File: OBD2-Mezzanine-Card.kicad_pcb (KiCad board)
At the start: 2 copper layers, 85 x 54 mm, 6 parts, among them P1 CONN_02X20, P2 CONN_02X20

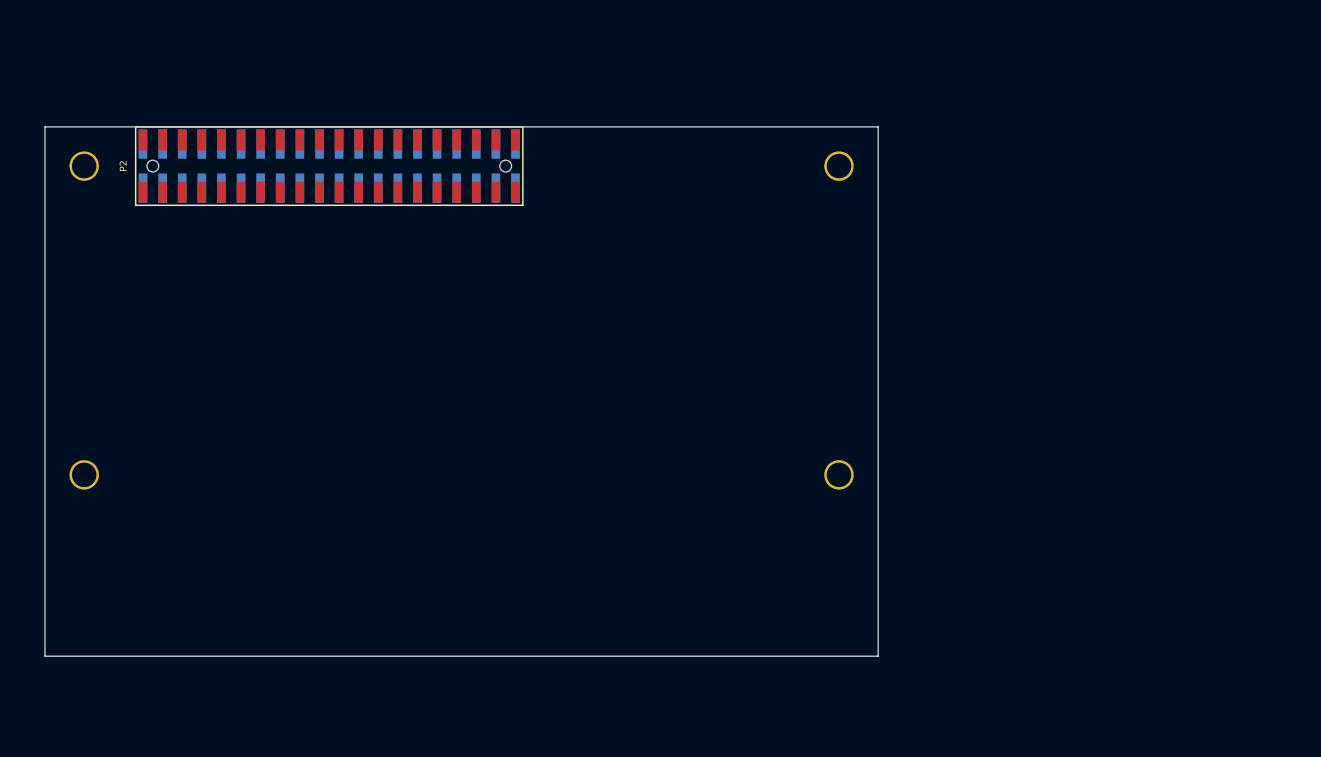
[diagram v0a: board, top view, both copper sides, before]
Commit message: kicad_pcd: Start to put the PCB together
Signed-off-by: Alistair Francis <alistair@alistair23.me>
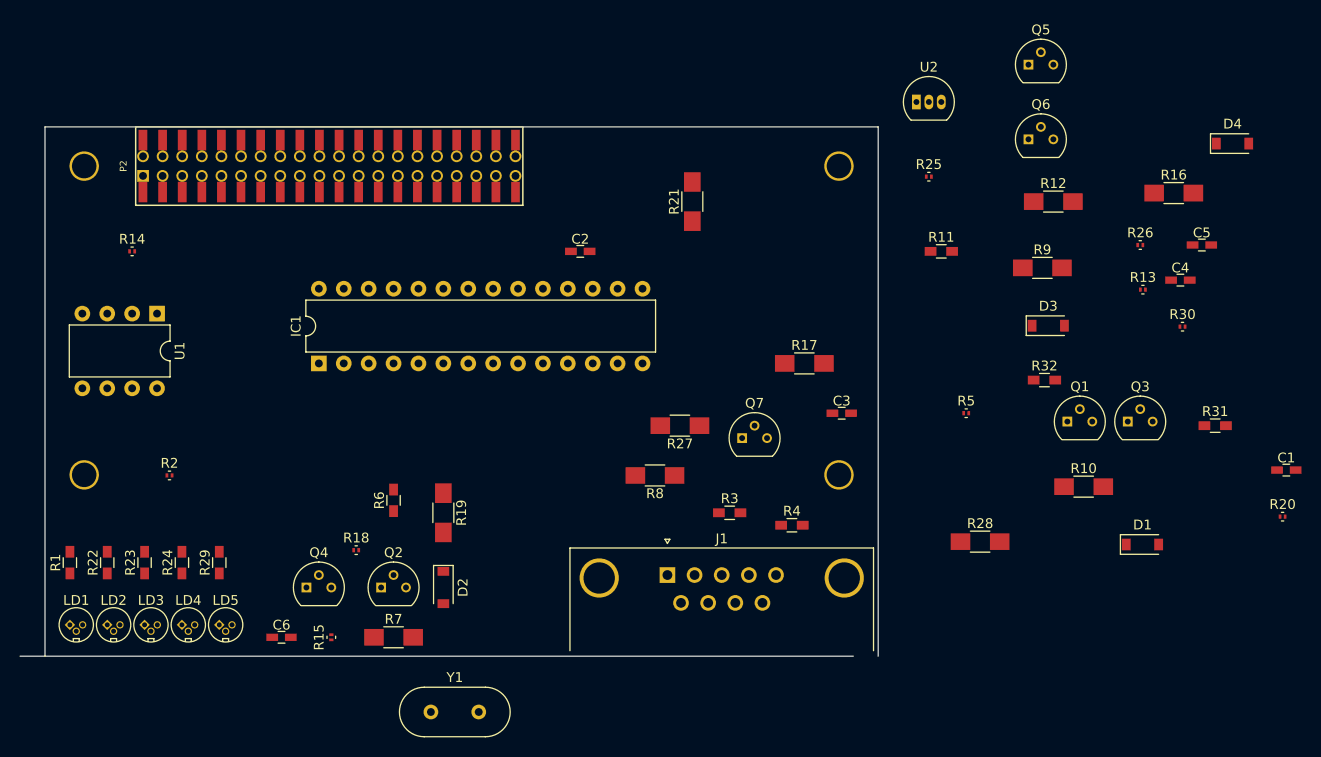
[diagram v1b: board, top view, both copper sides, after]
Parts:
- added C1: 0.1uF, Capacitors_SMD:C_0603_HandSoldering, F.Cu at (226.6, 135.0)
- added C2: 560pF, Capacitors_SMD:C_0603_HandSoldering, F.Cu at (154.6, 112.7)
- added C3: 560pF, Capacitors_SMD:C_0603_HandSoldering, F.Cu at (181.3, 129.2)
- added C4: 27pF, Capacitors_SMD:C_0603_HandSoldering, F.Cu at (215.8, 115.6)
- added C5: 27pF, Capacitors_SMD:C_0603_HandSoldering, F.Cu at (218.0, 112.1)
- added C6: 0.1uF, Capacitors_SMD:C_0603_HandSoldering, F.Cu at (124.1, 152.1)
- added D1: D, Diodes_SMD:D_SOD-123, F.Cu at (212.0, 142.6)
- added D2: D, Diodes_SMD:D_SOD-123, F.Cu at (140.6, 147.0)
- added D3: D, Diodes_SMD:D_SOD-123, F.Cu at (202.4, 120.3)
- added D4: D, Diodes_SMD:D_SOD-123, F.Cu at (221.2, 101.7)
- added IC1: ELM327, Housings_DIP:DIP-28_W7.62mm, F.Cu at (127.9, 124.1)
- added J1: OBD2-DB9_Male, Connectors_DSub:DSUB-9_Male_Horizontal_Pitch2.77x2.84mm_EdgePinOffset4.94mm_Housed_MountingHolesOffset7.48mm, F.Cu at (163.5, 145.7)
- added LD1: LD_1C2A, Opto-Devices:LaserDiode_TO3.3(D3.3)-3, F.Cu at (102.5, 150.8)
- added LD2: LD_1C2A, Opto-Devices:LaserDiode_TO3.3(D3.3)-3, F.Cu at (106.3, 150.8)
- added LD3: LD_1C2A, Opto-Devices:LaserDiode_TO3.3(D3.3)-3, F.Cu at (110.2, 150.8)
- added LD4: LD_1C2A, Opto-Devices:LaserDiode_TO3.3(D3.3)-3, F.Cu at (114.0, 150.8)
- added LD5: LD_1C2A, Opto-Devices:LaserDiode_TO3.3(D3.3)-3, F.Cu at (117.8, 150.8)
- added Q1: 2N3904, TO_SOT_Packages_THT:TO-92_Molded_Narrow, F.Cu at (204.3, 130.1)
- added Q2: 2N3906, TO_SOT_Packages_THT:TO-92_Molded_Narrow, F.Cu at (134.3, 147.0)
- added Q3: 2N3906, TO_SOT_Packages_THT:TO-92_Molded_Narrow, F.Cu at (210.5, 130.1)
- added Q4: 2N3904, TO_SOT_Packages_THT:TO-92_Molded_Narrow, F.Cu at (126.7, 147.0)
- added Q5: 2N3904, TO_SOT_Packages_THT:TO-92_Molded_Narrow, F.Cu at (200.3, 93.7)
- added Q6: 2N3904, TO_SOT_Packages_THT:TO-92_Molded_Narrow, F.Cu at (200.3, 101.3)
- added Q7: 2N3904, TO_SOT_Packages_THT:TO-92_Molded_Narrow, F.Cu at (171.1, 131.8)
- added R1: 470, Resistors_SMD:R_0603_HandSoldering, F.Cu at (102.5, 144.4)
- added R10: 10K, Resistors_SMD:R_1206_HandSoldering, F.Cu at (206.0, 136.7)
- added R11: 470, Resistors_SMD:R_0603_HandSoldering, F.Cu at (191.4, 112.7)
- added R12: 47K, Resistors_SMD:R_1206_HandSoldering, F.Cu at (202.9, 107.6)
- added R13: 2.2K, Resistors_SMD:R_0201, F.Cu at (212.0, 116.6)
- added R14: 1.8K, Resistors_SMD:R_0201, F.Cu at (108.9, 112.7)
- added R15: 4.7K, Resistors_SMD:R_0201, F.Cu at (129.2, 152.1)
- added R16: 10K, Resistors_SMD:R_1206_HandSoldering, F.Cu at (215.2, 106.8)
- added R17: 10K, Resistors_SMD:R_1206_HandSoldering, F.Cu at (177.5, 124.1)
- added R18: 4.7K, Resistors_SMD:R_0201, F.Cu at (131.8, 143.2)
- added R19: 10K, Resistors_SMD:R_1206_HandSoldering, F.Cu at (140.6, 139.4)
- added R2: 4.7K, Resistors_SMD:R_0201, F.Cu at (112.7, 135.6)
- added R20: 4.7K, Resistors_SMD:R_0201, F.Cu at (226.3, 139.8)
- added R21: 22K, Resistors_SMD:R_1206_HandSoldering, F.Cu at (166.0, 107.6)
- added R22: 470, Resistors_SMD:R_0603_HandSoldering, F.Cu at (106.3, 144.4)
- added R23: 470, Resistors_SMD:R_0603_HandSoldering, F.Cu at (110.2, 144.4)
- added R24: 470, Resistors_SMD:R_0603_HandSoldering, F.Cu at (114.0, 144.4)
- added R25: 2.2K, Resistors_SMD:R_0201, F.Cu at (190.2, 105.1)
- added R26: 2.2K, Resistors_SMD:R_0201, F.Cu at (211.7, 112.1)
- added R27: 47K, Resistors_SMD:R_1206_HandSoldering, F.Cu at (164.8, 130.5)
- added R28: 33K, Resistors_SMD:R_1206_HandSoldering, F.Cu at (195.4, 142.3)
- added R29: 470, Resistors_SMD:R_0603_HandSoldering, F.Cu at (117.8, 144.4)
- added R3: 100, Resistors_SMD:R_0603_HandSoldering, F.Cu at (169.8, 139.4)
- added R30: 4.7K, Resistors_SMD:R_0201, F.Cu at (216.0, 120.4)
- added R31: 510, Resistors_SMD:R_0603_HandSoldering, F.Cu at (219.4, 130.5)
- added R32: 510, Resistors_SMD:R_0603_HandSoldering, F.Cu at (202.0, 125.8)
- added R4: 100, Resistors_SMD:R_0603_HandSoldering, F.Cu at (176.2, 140.6)
- added R5: 4.7K, Resistors_SMD:R_0201, F.Cu at (194.0, 129.2)
- added R6: 470, Resistors_SMD:R_0603_HandSoldering, F.Cu at (135.6, 138.1)
- added R7: 10K, Resistors_SMD:R_1206_HandSoldering, F.Cu at (135.6, 152.1)
- added R8: 22K, Resistors_SMD:R_1206_HandSoldering, F.Cu at (162.2, 135.6)
- added R9: 47K, Resistors_SMD:R_1206_HandSoldering, F.Cu at (201.8, 114.4)
- added U1: MCP2561-E/P, Housings_DIP:DIP-8_W7.62mm, F.Cu at (111.4, 119.0)
- added U2: LM317L_TO92, TO_SOT_Packages_THT:TO-92_Inline_Narrow_Oval, F.Cu at (188.9, 97.5)
- added Y1: 4.0MHz, Crystals:Crystal_HC49-U_Vertical, F.Cu at (139.4, 159.7)
- P1: footprint 96boards:Pin_Header_SMD_2x20_Pitch2mm -> 96boards:Pin_Header_Straight_2x20_Pitch2mm
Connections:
- P1 pad 10: SPIO_DIN -> Net-(P1-Pad10)
- P1 pad 11: UART1_TX -> Net-(P1-Pad11)
- P1 pad 12: SPIO_CS -> Net-(P1-Pad12)
- P1 pad 13: UART1_RX -> Net-(P1-Pad13)
- P1 pad 14: SPIO_DOUT -> Net-(P1-Pad14)
- P1 pad 15: I2C0_SCL -> Net-(P1-Pad15)
- P1 pad 16: PCM_FS -> Net-(P1-Pad16)
- P1 pad 17: I2C0_SDA -> Net-(P1-Pad17)
- P1 pad 18: PCM_CLK -> Net-(P1-Pad18)
- P1 pad 19: I2C1_SCL -> Net-(P1-Pad19)
- P1 pad 20: PCM_DO -> Net-(P1-Pad20)
- P1 pad 21: I2C1_SDA -> Net-(P1-Pad21)
- P1 pad 22: PCM_DI -> Net-(P1-Pad22)
- P1 pad 23: GPIO_A -> Net-(P1-Pad23)
- P1 pad 24: GPIO_B -> Net-(P1-Pad24)
- P1 pad 25: GPIO_C -> Net-(P1-Pad25)
- P1 pad 26: GPIO_D -> Net-(P1-Pad26)
- P1 pad 27: GPIO_E -> Net-(P1-Pad27)
- P1 pad 28: GPIO_F -> Net-(P1-Pad28)
- P1 pad 29: GPIO_G -> Net-(P1-Pad29)
- P1 pad 3: UART0_CTS -> Net-(P1-Pad3)
- P1 pad 30: GPIO_H -> Net-(P1-Pad30)
- P1 pad 31: GPIO_I -> Net-(P1-Pad31)
- P1 pad 32: GPIO_J -> Net-(P1-Pad32)
- P1 pad 33: GPIO_K -> Net-(P1-Pad33)
- P1 pad 34: GPIO_L -> Net-(P1-Pad34)
- P1 pad 35: +1V8 -> Net-(P1-Pad35)
- P1 pad 36: SYS_DCIN -> Net-(P1-Pad36)
- P1 pad 38: SYS_DCIN -> Net-(P1-Pad38)
- P1 pad 4: PWR_BTN_N -> Net-(P1-Pad4)
- P1 pad 6: RST_BTN_N -> Net-(P1-Pad6)
- P1 pad 8: SPIO_SCL -> Net-(P1-Pad8)
- P1 pad 9: UART0_RTS -> Net-(P1-Pad9)
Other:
- board size 85 x 54 mm -> 87.5 x 54 mm
